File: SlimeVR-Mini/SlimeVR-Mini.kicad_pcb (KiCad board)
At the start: 2 copper layers, 1 part, among them U1 ESP32-C3-MINI-1-N4

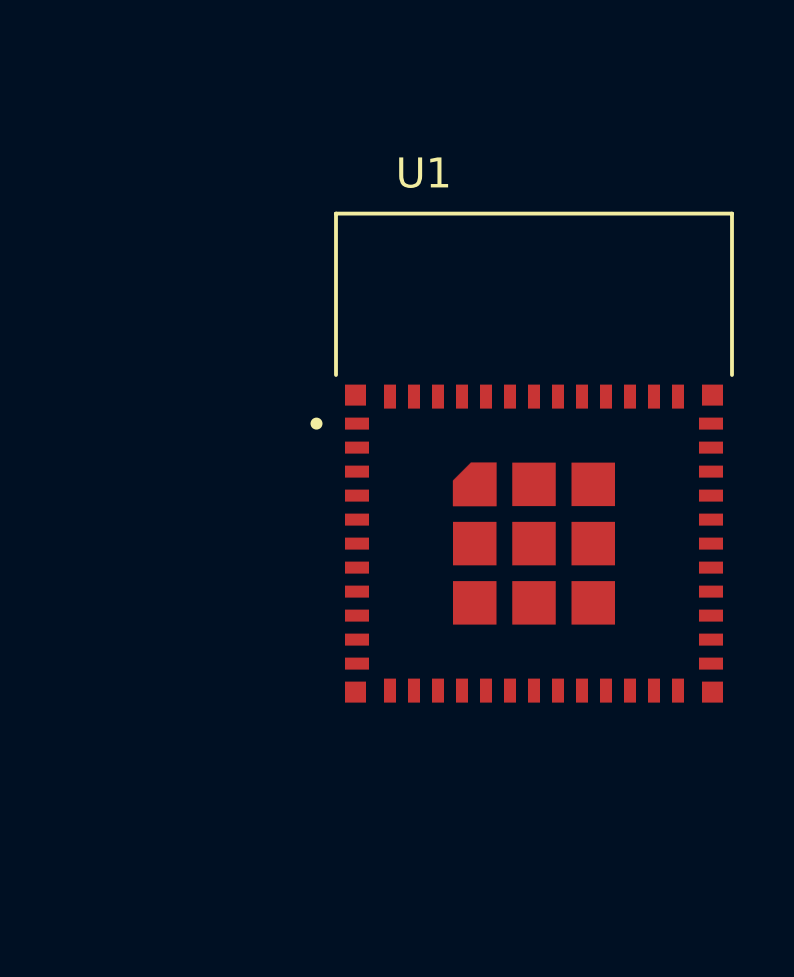
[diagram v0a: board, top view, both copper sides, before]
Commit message: added Power page + fixing symbols and footprints
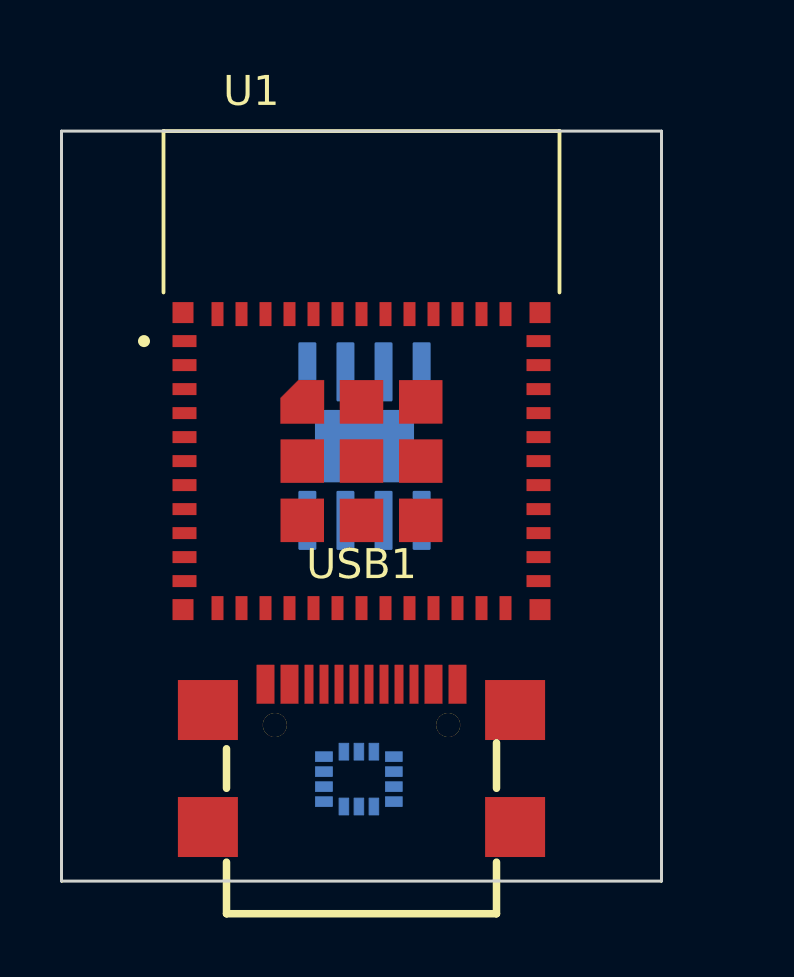
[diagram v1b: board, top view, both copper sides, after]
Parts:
- added U2: BMI160, Project Library:PQFN50P250X300X88-14N, B.Cu at (149.9, 111.6)
- added U3: TP4056, Project Library:SOP127P600X175-9N, B.Cu at (150.1, 100.5)
- added USB1: TYPEC-304YSSW-ACP16, Project Library:USB-SMD_TYPEC-304YSSW-ACP16, F.Cu at (150.0, 110.8)
- moved U1 6.37 mm to (150.0, 98.3)
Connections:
- net Net-(U1-GND-Pad1) renamed GND
- U1 pad 22: unconnected-(U1-IO8-Pad22) -> Net-(U1-IO8)
- U1 pad 23: unconnected-(U1-IO9-Pad23) -> /Microcontroller/BOOT
- U1 pad 3: unconnected-(U1-3V3-Pad3) -> +3V3
- U1 pad 5: unconnected-(U1-IO2-Pad5) -> /Microcontroller/BATT ADC
- U1 pad 8: unconnected-(U1-EN-Pad8) -> /Microcontroller/ESP EN
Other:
- board outline added: 20 x 25 mm

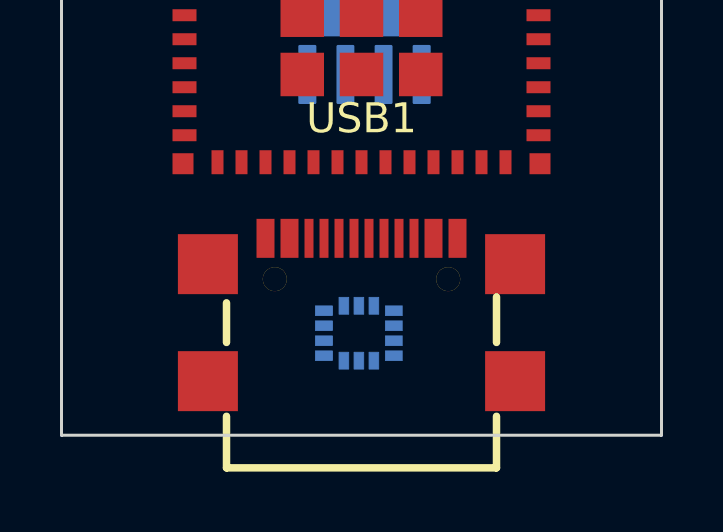
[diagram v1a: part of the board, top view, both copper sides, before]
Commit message: added CH340N + schematics development
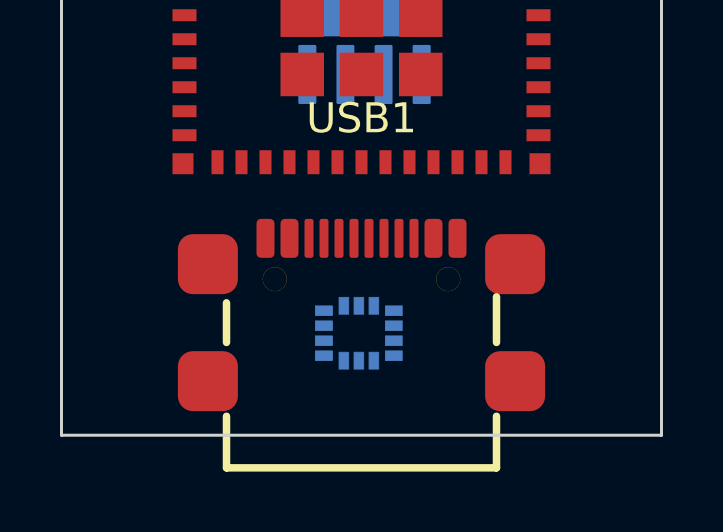
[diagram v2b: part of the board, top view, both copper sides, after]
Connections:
- USB1 pad 13: unconnected-(USB1-GND-Pad13) -> Net-(C5-Pad1)
- USB1 pad 14: unconnected-(USB1-GND-Pad14) -> Net-(C5-Pad1)
- USB1 pad 15: unconnected-(USB1-GND-Pad15) -> Net-(C5-Pad1)
- USB1 pad 16: unconnected-(USB1-GND-Pad16) -> Net-(C5-Pad1)
- USB1 pad A1B12: unconnected-(USB1-GND-PadA1B12) -> GND
- USB1 pad A4B9: unconnected-(USB1-VBUS-PadA4B9) -> VBUS
- USB1 pad A5: unconnected-(USB1-CC1-PadA5) -> Net-(USB1-CC1)
- USB1 pad A6: unconnected-(USB1-DP1-PadA6) -> /Power/D+
- USB1 pad A7: unconnected-(USB1-DN1-PadA7) -> /Power/D-
- USB1 pad B1A12: unconnected-(USB1-GND-PadB1A12) -> GND
- USB1 pad B4A9: unconnected-(USB1-VBUS-PadB4A9) -> VBUS
- USB1 pad B5: unconnected-(USB1-CC2-PadB5) -> Net-(USB1-CC2)
- USB1 pad B6: unconnected-(USB1-DP2-PadB6) -> /Power/D+
- USB1 pad B7: unconnected-(USB1-DN2-PadB7) -> /Power/D-
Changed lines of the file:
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@@
   (net 50 "unconnected-(U3-CE-Pad8)")
   (net 51 "unconnected-(U3-EP-Pad9)")
-  (net 52 "unconnected-(USB1-GND-Pad13)")
-  (net 53 "unconnected-(USB1-GND-Pad14)")
-  (net 54 "unconnected-(USB1-GND-Pad15)")
-  (net 55 "unconnected-(USB1-GND-Pad16)")
-  (net 56 "unconnected-(USB1-GND-PadA1B12)")
-  (net 57 "unconnected-(USB1-VBUS-PadA4B9)")
-  (net 58 "unconnected-(USB1-CC1-PadA5)")
-  (net 59 "unconnected-(USB1-DP1-PadA6)")
-  (net 60 "unconnected-(USB1-DN1-PadA7)")
-  (net 61 "unconnected-(USB1-SBU1-PadA8)")
-  (net 62 "unconnected-(USB1-GND-PadB1A12)")
-  (net 63 "unconnected-(USB1-VBUS-PadB4A9)")
-  (net 64 "unconnected-(USB1-CC2-PadB5)")
-  (net 65 "unconnected-(USB1-DP2-PadB6)")
-  (net 66 "unconnected-(USB1-DN2-PadB7)")
-  (net 67 "unconnected-(USB1-SBU2-PadB8)")
+  (net 52 "VBUS")
+  (net 53 "Net-(USB1-CC1)")
+  (net 54 "Net-(USB1-CC2)")
+  (net 55 "Net-(C5-Pad1)")
+  (net 56 "/Power/D+")
+  (net 57 "unconnected-(USB1-SBU1-PadA8)")
+  (net 58 "/Power/D-")
+  (net 59 "unconnected-(USB1-SBU2-PadB8)")
   (footprint "Project Library:USB-SMD_TYPEC-304YSSW-ACP16" (layer "F.Cu")
     (at 150 110.8175)
@@
     (pad "" thru_hole circle (at -2.89 -1.02) (size 0.8 0.8) (drill 0.8) (layers "*.Cu" "*.Mask"))
     (pad "" thru_hole circle (at 2.89 -1.02) (size 0.8 0.8) (drill 0.8) (layers "*.Cu" "*.Mask"))
-    (pad "13" smd rect (at -5.12 -1.52) (size 2 2) (layers "F.Cu" "F.Paste" "F.Mask")
-      (net 52 "unconnected-(USB1-GND-Pad13)") (pinfunction "GND") (pintype "unspecified"))
-    (pad "14" smd rect (at 5.12 -1.52) (size 2 2) (layers "F.Cu" "F.Paste" "F.Mask")
-      (net 53 "unconnected-(USB1-GND-Pad14)") (pinfunction "GND") (pintype "unspecified"))
-    (pad "15" smd rect (at -5.12 2.38) (size 2 2) (layers "F.Cu" "F.Paste" "F.Mask")
-      (net 54 "unconnected-(USB1-GND-Pad15)") (pinfunction "GND") (pintype "unspecified"))
-    (pad "16" smd rect (at 5.12 2.38) (size 2 2) (layers "F.Cu" "F.Paste" "F.Mask")
-      (net 55 "unconnected-(USB1-GND-Pad16)") (pinfunction "GND") (pintype "unspecified"))
-    (pad "A1B12" smd rect (at -3.2 -2.38) (size 0.6 1.3) (layers "F.Cu" "F.Paste" "F.Mask")
-      (net 56 "unconnected-(USB1-GND-PadA1B12)") (pinfunction "GND") (pintype "unspecified"))
-    (pad "A4B9" smd rect (at -2.4 -2.38) (size 0.6 1.3) (layers "F.Cu" "F.Paste" "F.Mask")
-      (net 57 "unconnected-(USB1-VBUS-PadA4B9)") (pinfunction "VBUS") (pintype "unspecified"))
-    (pad "A5" smd rect (at -1.25 -2.38) (size 0.3 1.3) (layers "F.Cu" "F.Paste" "F.Mask")
-      (net 58 "unconnected-(USB1-CC1-PadA5)") (pinfunction "CC1") (pintype "unspecified"))
-    (pad "A6" smd rect (at -0.25 -2.38) (size 0.3 1.3) (layers "F.Cu" "F.Paste" "F.Mask")
-      (net 59 "unconnected-(USB1-DP1-PadA6)") (pinfunction "DP1") (pintype "unspecified"))
-    (pad "A7" smd rect (at 0.25 -2.38) (size 0.3 1.3) (layers "F.Cu" "F.Paste" "F.Mask")
-      (net 60 "unconnected-(USB1-DN1-PadA7)") (pinfunction "DN1") (pintype "unspecified"))
-    (pad "A8" smd rect (at 1.25 -2.38) (size 0.3 1.3) (layers "F.Cu" "F.Paste" "F.Mask")
-      (net 61 "unconnected-(USB1-SBU1-PadA8)") (pinfunction "SBU1") (pintype "unspecified"))
-    (pad "B1A12" smd rect (at 3.2 -2.38) (size 0.6 1.3) (layers "F.Cu" "F.Paste" "F.Mask")
-      (net 62 "unconnected-(USB1-GND-PadB1A12)") (pinfunction "GND") (pintype "unspecified"))
-    (pad "B4A9" smd rect (at 2.4 -2.38) (size 0.6 1.3) (layers "F.Cu" "F.Paste" "F.Mask")
-      (net 63 "unconnected-(USB1-VBUS-PadB4A9)") (pinfunction "VBUS") (pintype "unspecified"))
-    (pad "B5" smd rect (at 1.75 -2.38) (size 0.3 1.3) (layers "F.Cu" "F.Paste" "F.Mask")
-      (net 64 "unconnected-(USB1-CC2-PadB5)") (pinfunction "CC2") (pintype "unspecified"))
-    (pad "B6" smd rect (at 0.75 -2.38) (size 0.3 1.3) (layers "F.Cu" "F.Paste" "F.Mask")
-      (net 65 "unconnected-(USB1-DP2-PadB6)") (pinfunction "DP2") (pintype "unspecified"))
-    (pad "B7" smd rect (at -0.75 -2.38) (size 0.3 1.3) (layers "F.Cu" "F.Paste" "F.Mask")
-      (net 66 "unconnected-(USB1-DN2-PadB7)") (pinfunction "DN2") (pintype "unspecified"))
-    (pad "B8" smd rect (at -1.75 -2.38) (size 0.3 1.3) (layers "F.Cu" "F.Paste" "F.Mask")
-      (net 67 "unconnected-(USB1-SBU2-PadB8)") (pinfunction "SBU2") (pintype "unspecified"))
+    (pad "13" smd roundrect (at -5.12 -1.52) (size 2 2) (layers "F.Cu" "F.Paste" "F.Mask") (roundrect_rratio 0.25)
+      (net 55 "Net-(C5-Pad1)") (pinfunction "GND") (pintype "unspecified"))
+    (pad "14" smd roundrect (at 5.12 -1.52) (size 2 2) (layers "F.Cu" "F.Paste" "F.Mask") (roundrect_rratio 0.25)
+      (net 55 "Net-(C5-Pad1)") (pinfunction "GND") (pintype "unspecified"))
+    (pad "15" smd roundrect (at -5.12 2.38) (size 2 2) (layers "F.Cu" "F.Paste" "F.Mask") (roundrect_rratio 0.25)
+      (net 55 "Net-(C5-Pad1)") (pinfunction "GND") (pintype "unspecified"))
+    (pad "16" smd roundrect (at 5.12 2.38) (size 2 2) (layers "F.Cu" "F.Paste" "F.Mask") (roundrect_rratio 0.25)
+      (net 55 "Net-(C5-Pad1)") (pinfunction "GND") (pintype "unspecified"))
+    (pad "A1B12" smd roundrect (at -3.2 -2.38) (size 0.6 1.3) (layers "F.Cu" "F.Paste" "F.Mask") (roundrect_rratio 0.25)
+      (net 28 "GND") (pinfunction "GND") (pintype "unspecified"))
+    (pad "A4B9" smd roundrect (at -2.4 -2.38) (size 0.6 1.3) (layers "F.Cu" "F.Paste" "F.Mask") (roundrect_rratio 0.25)
+      (net 52 "VBUS") (pinfunction "VBUS") (pintype "unspecified"))
+    (pad "A5" smd roundrect (at -1.25 -2.38) (size 0.3 1.3) (layers "F.Cu" "F.Paste" "F.Mask") (roundrect_rratio 0.25)
+      (net 53 "Net-(USB1-CC1)") (pinfunction "CC1") (pintype "unspecified"))
+    (pad "A6" smd roundrect (at -0.25 -2.38) (size 0.3 1.3) (layers "F.Cu" "F.Paste" "F.Mask") (roundrect_rratio 0.25)
+      (net 56 "/Power/D+") (pinfunction "DP1") (pintype "unspecified"))
+    (pad "A7" smd roundrect (at 0.25 -2.38) (size 0.3 1.3) (layers "F.Cu" "F.Paste" "F.Mask") (roundrect_rratio 0.25)
+      (net 58 "/Power/D-") (pinfunction "DN1") (pintype "unspecified"))
+    (pad "A8" smd roundrect (at 1.25 -2.38) (size 0.3 1.3) (layers "F.Cu" "F.Paste" "F.Mask") (roundrect_rratio 0.25)
+      (net 57 "unconnected-(USB1-SBU1-PadA8)") (pinfunction "SBU1") (pintype "unspecified+no_connect"))
+    (pad "B1A12" smd roundrect (at 3.2 -2.38) (size 0.6 1.3) (layers "F.Cu" "F.Paste" "F.Mask") (roundrect_rratio 0.25)
+      (net 28 "GND") (pinfunction "GND") (pintype "unspecified"))
+    (pad "B4A9" smd roundrect (at 2.4 -2.38) (size 0.6 1.3) (layers "F.Cu" "F.Paste" "F.Mask") (roundrect_rratio 0.25)
+      (net 52 "VBUS") (pinfunction "VBUS") (pintype "unspecified"))
+    (pad "B5" smd roundrect (at 1.75 -2.38) (size 0.3 1.3) (layers "F.Cu" "F.Paste" "F.Mask") (roundrect_rratio 0.25)
+      (net 54 "Net-(USB1-CC2)") (pinfunction "CC2") (pintype "unspecified"))
+    (pad "B6" smd roundrect (at 0.75 -2.38) (size 0.3 1.3) (layers "F.Cu" "F.Paste" "F.Mask") (roundrect_rratio 0.25)
+      (net 56 "/Power/D+") (pinfunction "DP2") (pintype "unspecified"))
+    (pad "B7" smd roundrect (at -0.75 -2.38) (size 0.3 1.3) (layers "F.Cu" "F.Paste" "F.Mask") (roundrect_rratio 0.25)
+      (net 58 "/Power/D-") (pinfunction "DN2") (pintype "unspecified"))
+    (pad "B8" smd roundrect (at -1.75 -2.38) (size 0.3 1.3) (layers "F.Cu" "F.Paste" "F.Mask") (roundrect_rratio 0.25)
+      (net 59 "unconnected-(USB1-SBU2-PadB8)") (pinfunction "SBU2") (pintype "unspecified+no_connect"))
     (model "${KIPRJMOD}/3D-Models/USB-SMD_TYPEC-304YSSW-ACP16.wrl"
       (offset (xyz 0 -1.5 0))

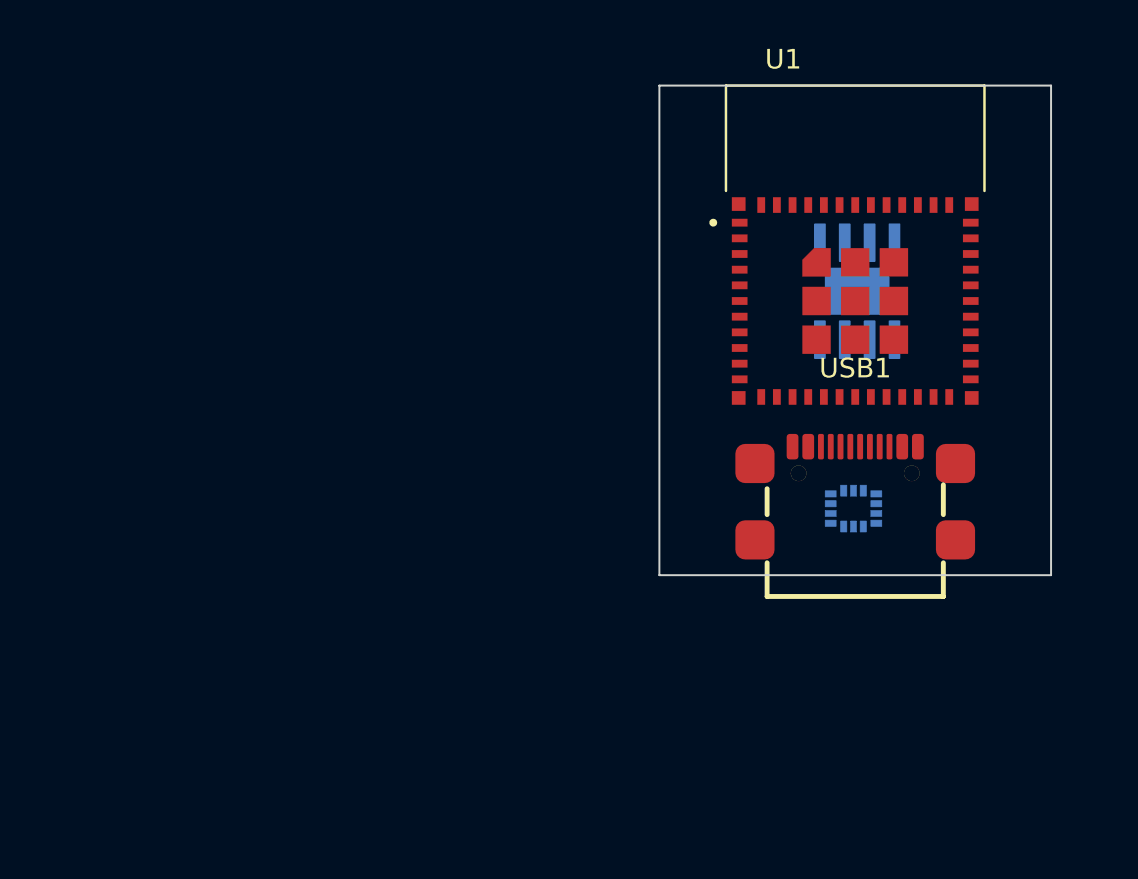
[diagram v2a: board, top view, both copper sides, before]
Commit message: assigned footprints, finished USB-UART sch
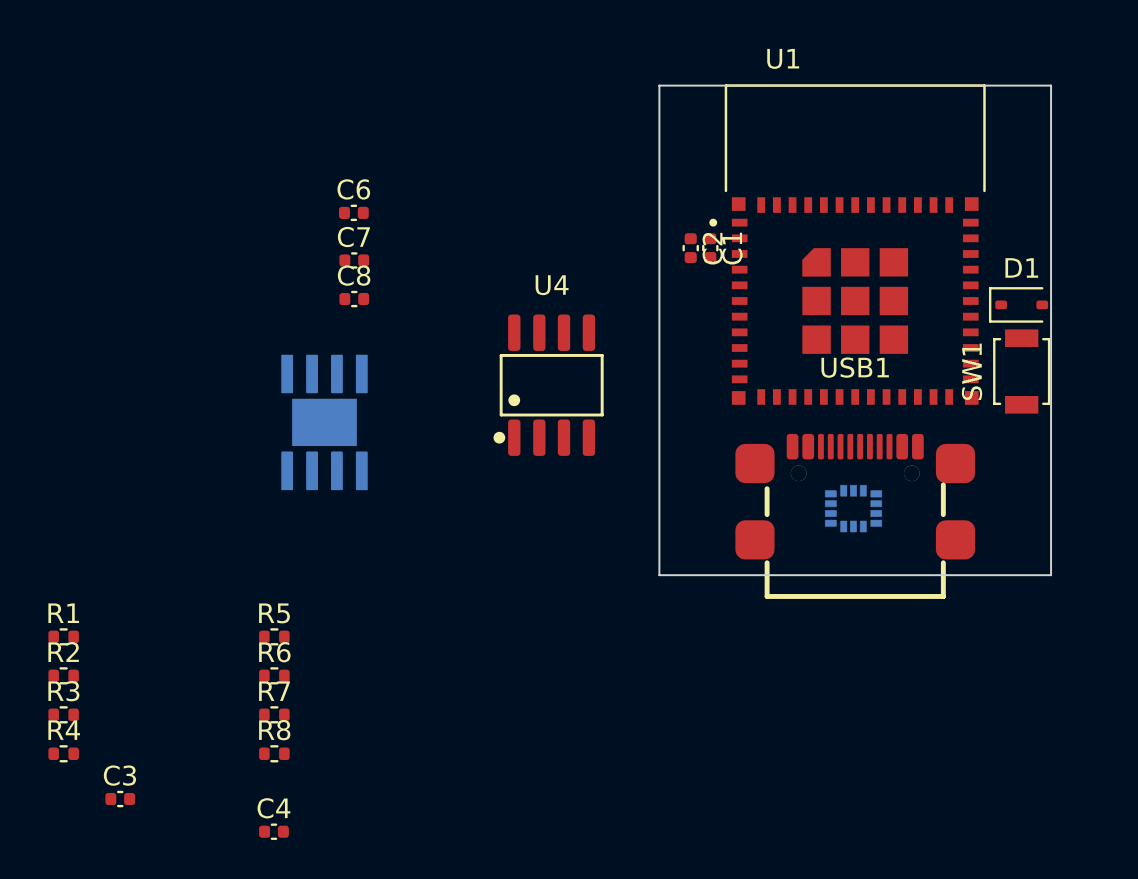
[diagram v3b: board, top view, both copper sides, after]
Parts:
- added C1: 10u, Capacitor_SMD:C_0402_1005Metric, F.Cu at (142.6, 98.3)
- added C2: 100n, Capacitor_SMD:C_0402_1005Metric, F.Cu at (141.6, 98.3)
- added C3: 1u, Capacitor_SMD:C_0402_1005Metric, F.Cu at (112.5, 126.4)
- added C4: 100n, Capacitor_SMD:C_0402_1005Metric, F.Cu at (120.3, 128.1)
- added C6: 100n, Capacitor_SMD:C_0402_1005Metric, F.Cu at (124.4, 96.5)
- added C7: 10u, Capacitor_SMD:C_0402_1005Metric, F.Cu at (124.4, 98.9)
- added C8: 100n, Capacitor_SMD:C_0402_1005Metric, F.Cu at (124.4, 100.9)
- added D1: 1N5819WS, Diode_SMD:D_SOD-323, F.Cu at (158.5, 101.2)
- added R1: 10k, Resistor_SMD:R_0402_1005Metric, F.Cu at (109.6, 118.2)
- added R2: 40k, Resistor_SMD:R_0402_1005Metric, F.Cu at (109.6, 120.1)
- added R3: 10k, Resistor_SMD:R_0402_1005Metric, F.Cu at (109.6, 122.1)
- added R4: 10k, Resistor_SMD:R_0402_1005Metric, F.Cu at (109.6, 124.1)
- added R5: 5k1, Resistor_SMD:R_0402_1005Metric, F.Cu at (120.3, 118.2)
- added R6: 5k1, Resistor_SMD:R_0402_1005Metric, F.Cu at (120.3, 120.1)
- added R7: 1M, Resistor_SMD:R_0402_1005Metric, F.Cu at (120.3, 122.1)
- added R8: ??k, Resistor_SMD:R_0402_1005Metric, F.Cu at (120.3, 124.1)
- added SW1: SW_Push, Button_Switch_SMD:SW_SPST_B3U-1000P, F.Cu at (158.5, 104.6)
- added U4: CH340N, Project Library:SOP-8_L4.9-W3.9-P1.27-LS6.0-BL, F.Cu at (134.5, 105.3)
- U1: footprint Project Library:XCVR_ESP32-C3-MINI-1-N4 -> Project Library:ESP32-C3-MINI-1-N4
- moved U3 28.0 mm to (122.9, 107.2)
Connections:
- U1 pad 30: unconnected-(U1-RXD0-Pad30) -> Net-(U1-RXD0)
- U1 pad 31: unconnected-(U1-TXD0-Pad31) -> Net-(D1-K)
- U3 pad 2: unconnected-(U3-PROG-Pad2) -> Net-(U3-PROG)
- U3 pad 3: unconnected-(U3-GND-Pad3) -> GND
- U3 pad 5: unconnected-(U3-BAT-Pad5) -> +BATT
